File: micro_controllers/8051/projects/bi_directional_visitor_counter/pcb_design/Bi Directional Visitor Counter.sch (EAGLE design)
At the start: 27 parts, among them IC1 AT89S51, IC2 7805TV

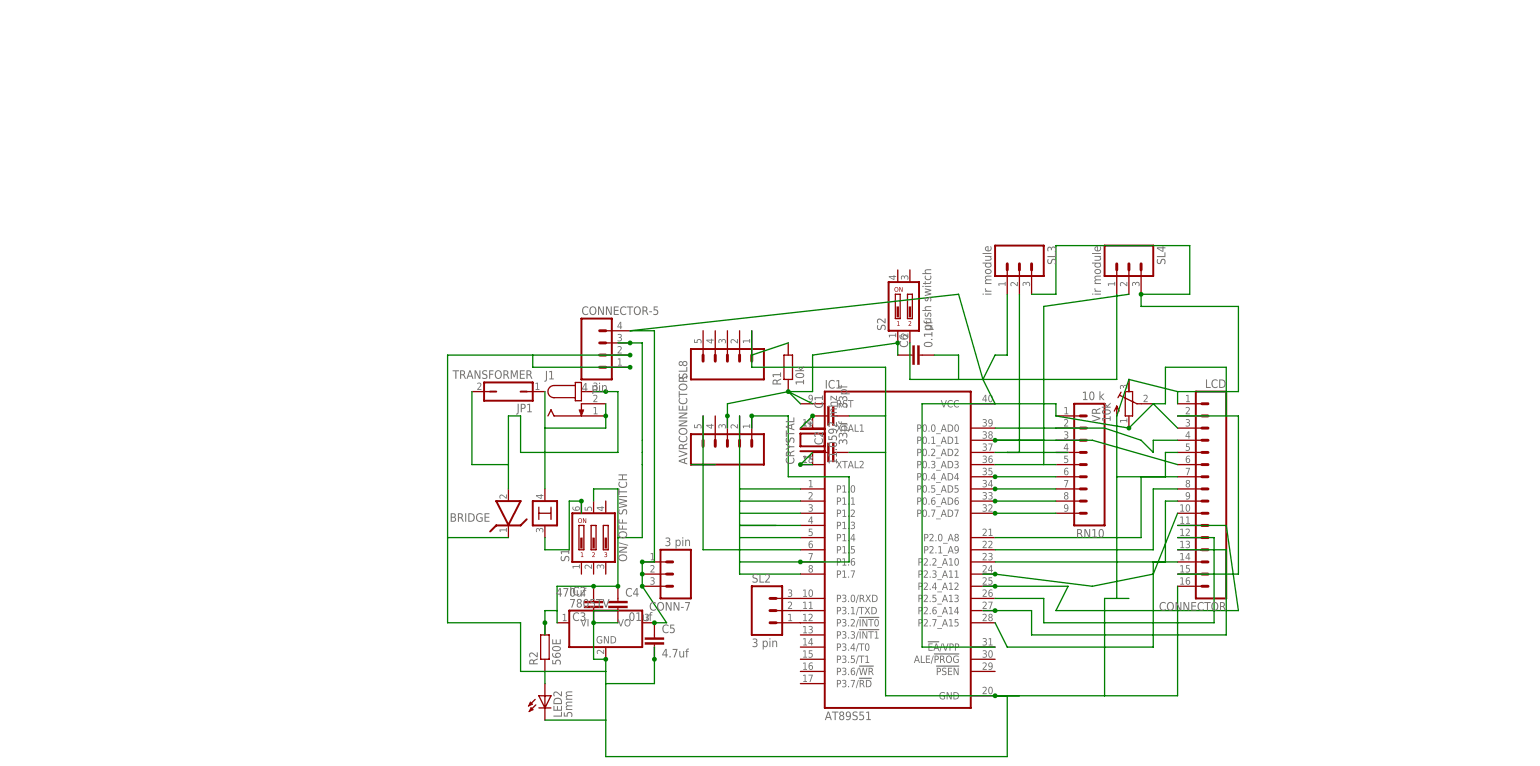
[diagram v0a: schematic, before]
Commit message: 
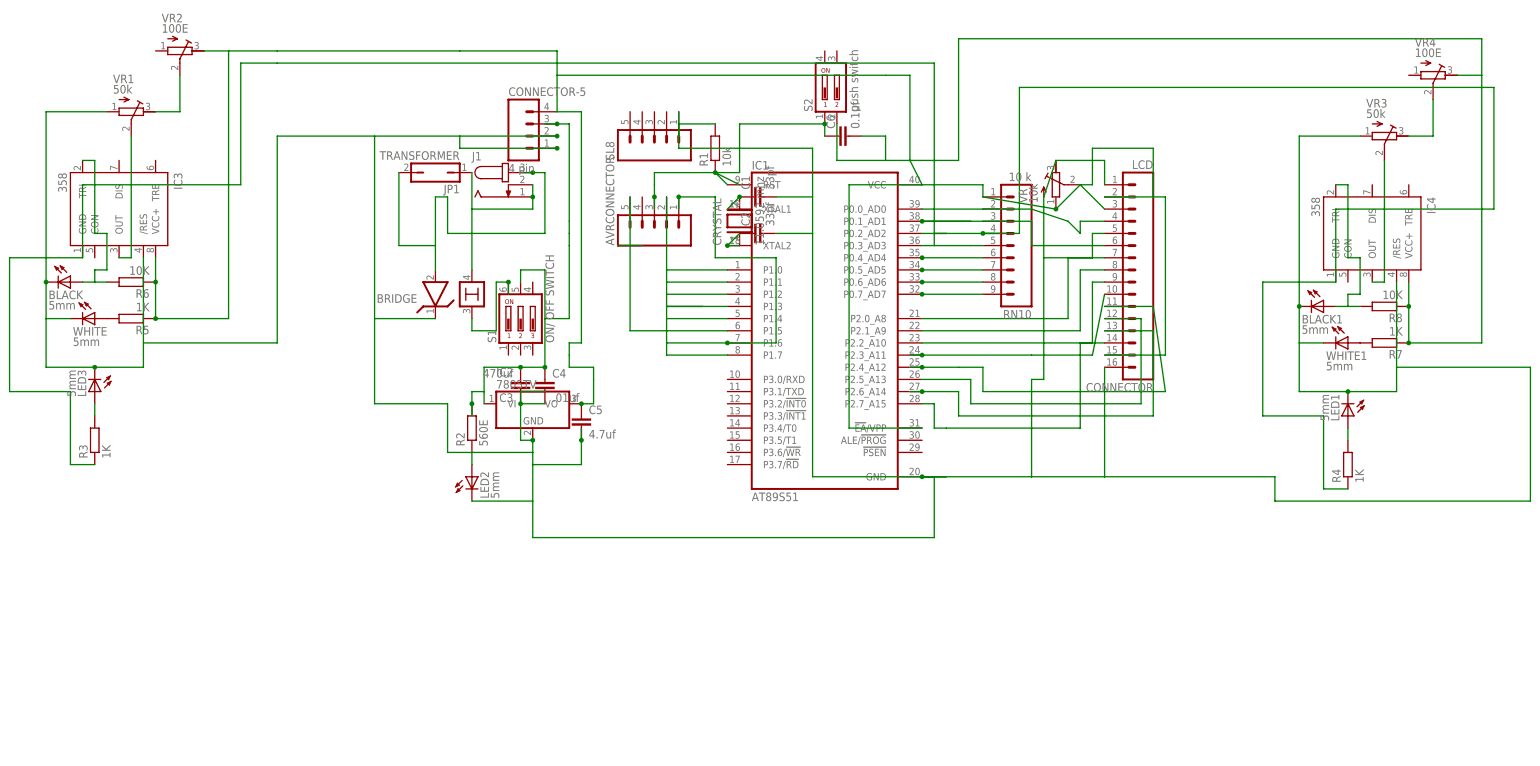
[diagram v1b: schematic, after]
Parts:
- removed CONN-7, SL2: 3 pin, con-amp-quick:M03
- removed SL3, SL4: ir module, con-amp-quick:M03
- added BLACK, BLACK1, LED1, LED3, WHITE, WHITE1: 5mm, led:LED5MM
- added IC3, IC4: 358, st-microelectronics:NE555
- added R3, R4, R5, R7: 1K, rcl:R-EU_0204/7
- added R6, R8: 10K, rcl:R-EU_0204/7
- added VR1, VR3: 50k, resistor:R-TRIMM64P
- added VR2, VR4: 100E, resistor:R-TRIMM64P
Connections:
- removed net N$24: IC1.P0.2_AD2, SL3.2
- removed net N$25: IC1.P0.3_AD3, RN10.5, SL4.2
- removed net N$3: IC1.P3.2/!INT0, SL2.1
- removed net N$39: C5.1, C6.2, CONN-7.1, CONN-7.2, CONN-7.3, CONNECTOR-5.4, CONNECTOR.15, CONNECTOR.2, IC1.!EA!/VPP, IC1.VCC, IC2.VO, RN10.1, S2.2, SL3.1, SL4.1, VR.E
- removed net N$6 (its old number): IC1.P3.1/TXD, SL2.2
- removed net N$7: IC1.P3.0/RXD, SL2.3
- new net N$10: R5.2, WHITE.A
- new net N$11: BLACK.A, IC3.TRI, R6.2
- new net N$12: IC3.OUT, VR1.S
- new net N$13: VR1.A, VR2.S
- new net N$23: LED3.A, R3.2
- new net N$34: IC1.P0.2_AD2, IC4.GND, R4.1, RN10.4
- new net N$36: R7.2, WHITE1.A
- new net N$37: BLACK1.A, IC4.TRI, R8.2
- new net N$40: IC4.OUT, VR3.S
- new net N$44: VR3.A, VR4.S
- new net N$50: LED1.A, R4.2
- new net N$8: C5.1, C6.2, CONNECTOR-5.4, CONNECTOR.15, CONNECTOR.2, IC1.!EA!/VPP, IC1.VCC, IC2.VO, IC3.VCC+, IC4.VCC+, R5.1, R6.1, R7.1, R8.1, RN10.1, S2.2, VR.E, VR2.A, VR4.A
- new net N$9: IC1.P0.3_AD3, IC3.GND, R3.1, RN10.5
- net N$41: now also BLACK.C, BLACK1.C, IC3./RES, IC4./RES, LED1.C, LED3.C, VR1.E, VR3.E, WHITE.C, WHITE1.C; no longer SL3.3, SL4.3
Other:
- moved on the sheet: AVRCONNECTOR, BRIDGE, C1, C2, C3, C4, C5, C6, CONNECTOR, CONNECTOR-5, CRYSTAL, IC1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
